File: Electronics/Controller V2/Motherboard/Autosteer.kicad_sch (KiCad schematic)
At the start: 12 parts, among them Q1 2N7002, Q2 2N7002, U11 ADS1115IDGS

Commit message: Added WAS circuit.
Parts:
- D5, D6: value D_Zener -> 1N5819WS; footprint (none) -> Diode_SMD:D_SOD-323; LCSC (none) -> C191023
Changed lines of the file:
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@@
       (effects (font (size 1.27 1.27)) (justify left))
     )
-    (property "Value" "D_Zener" (at 117.475 90.805 90)
-      (effects (font (size 1.27 1.27)) (justify left) hide)
+    (property "Value" "1N5819WS" (at 111.76 81.915 0)
+      (effects (font (size 1.27 1.27)) (justify left))
     )
-    (property "Footprint" "" (at 114.3 89.535 0)
+    (property "Footprint" "Diode_SMD:D_SOD-323" (at 114.3 89.535 0)
       (effects (font (size 1.27 1.27)) hide)
     )
     (property "Datasheet" "~" (at 114.3 89.535 0)
+      (effects (font (size 1.27 1.27)) hide)
+    )
+    (property "LCSC" "C191023" (at 114.3 89.535 0)
       (effects (font (size 1.27 1.27)) hide)
     )
@@
       (effects (font (size 1.27 1.27)) (justify left))
     )
-    (property "Value" "D_Zener" (at 125.73 90.805 90)
-      (effects (font (size 1.27 1.27)) (justify left) hide)
+    (property "Value" "1N5819WS" (at 120.015 81.915 0)
+      (effects (font (size 1.27 1.27)) (justify left))
     )
-    (property "Footprint" "" (at 122.555 89.535 0)
+    (property "Footprint" "Diode_SMD:D_SOD-323" (at 122.555 89.535 0)
       (effects (font (size 1.27 1.27)) hide)
     )
@@
       (effects (font (size 1.27 1.27)) hide)
     )
+    (property "LCSC" "C191023" (at 122.555 89.535 0)
+      (effects (font (size 1.27 1.27)) hide)
+    )

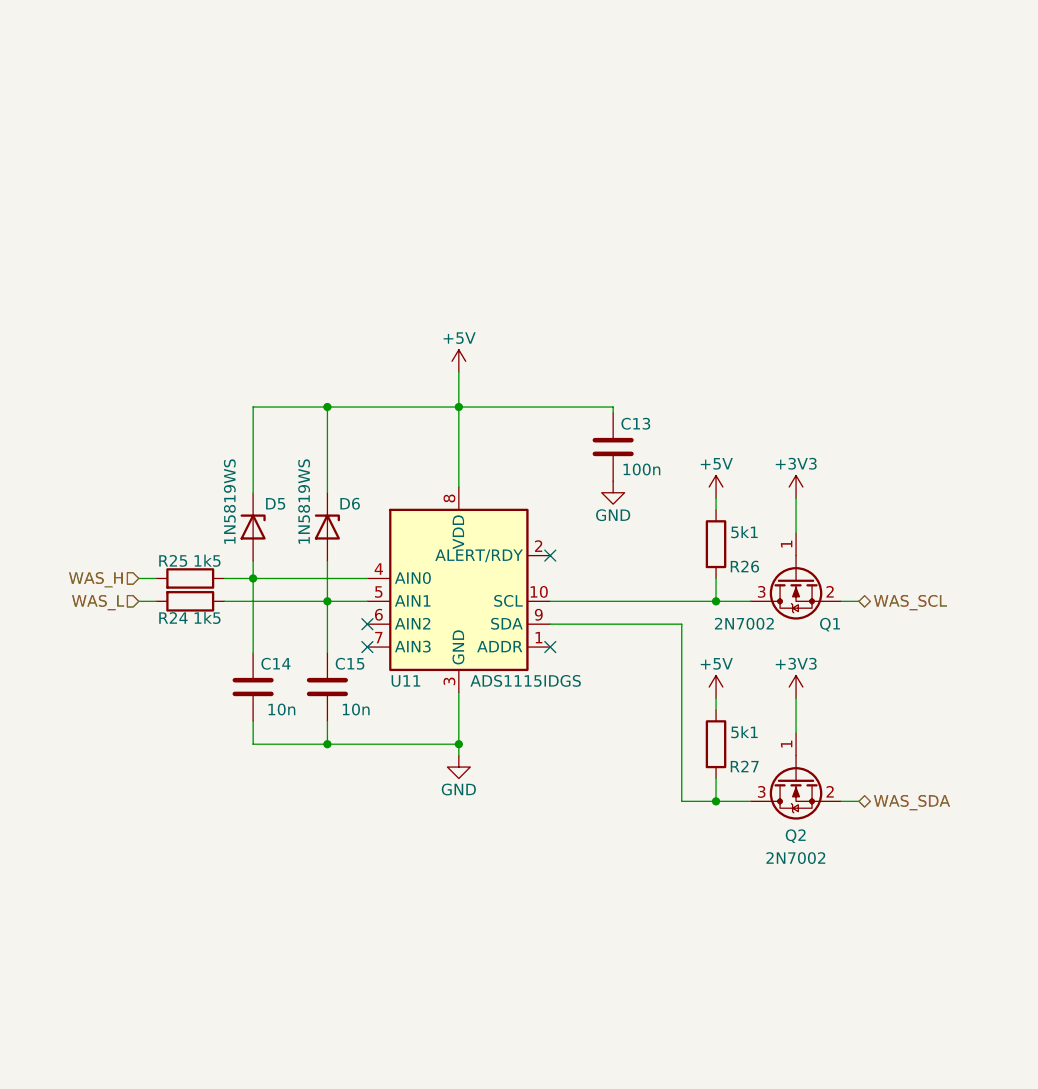
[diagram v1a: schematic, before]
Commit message: Added current sensing for valve E.
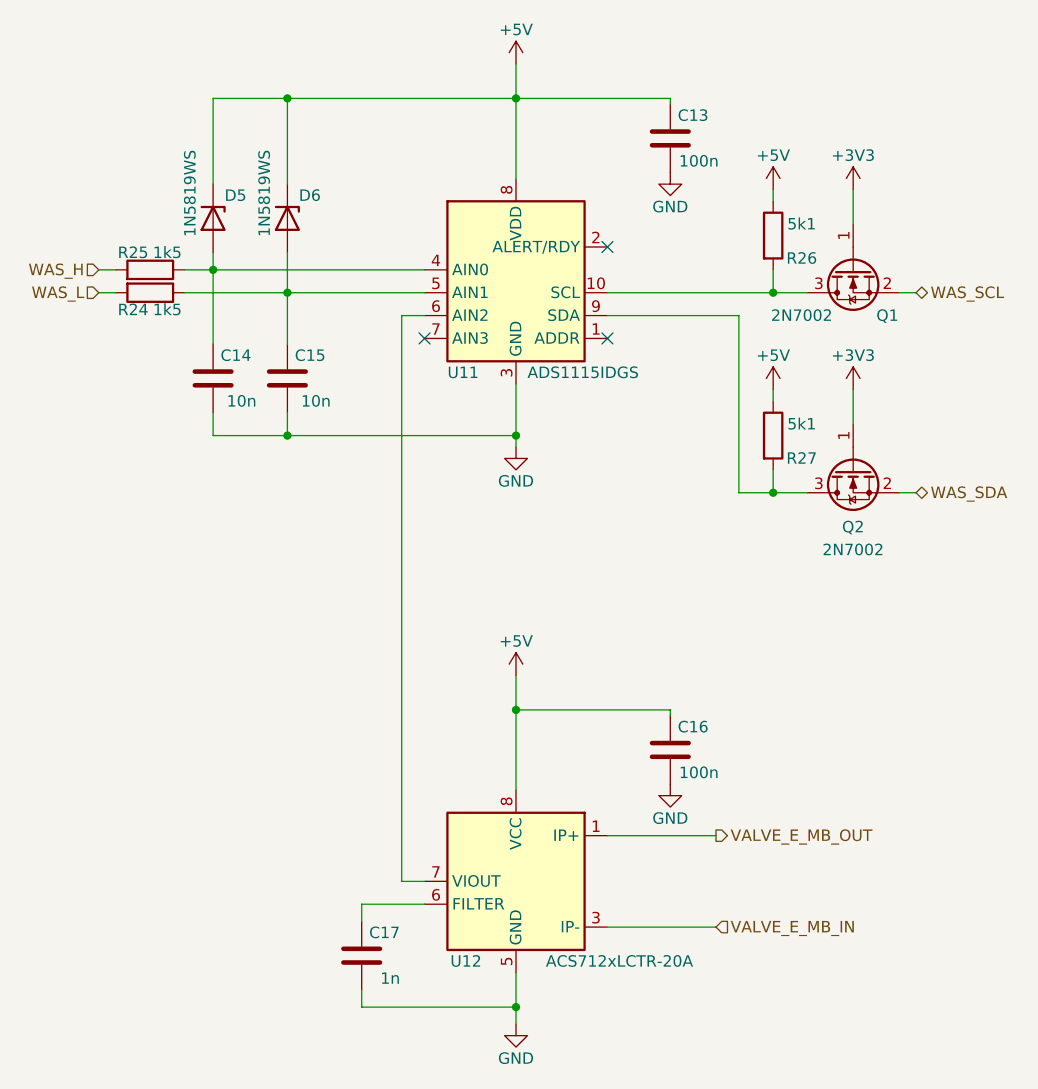
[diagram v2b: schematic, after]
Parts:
- added C16: 100n, Capacitor_SMD:C_0805_2012Metric, symbol Device:C
- added C17: 1n, Capacitor_SMD:C_0805_2012Metric, symbol Device:C
- added U12: ACS712xLCTR-20A, Package_SO:SOIC-8_3.9x4.9mm_P1.27mm, symbol Sensor_Current:ACS712xLCTR-20A
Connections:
- net +5V: now also C16.2, U12.8 (VCC)
- net GND: now also C16.1, C17.1, U12.5 (GND)
- net at U11.6 (AIN2): now also U12.7 (VIOUT)
- new net: C17.2, U12.6 (FILTER)
- new net VALVE_E_MB_IN: U12.3 (IP-), U12.4 (IP-)
- new net VALVE_E_MB_OUT: U12.1 (IP+), U12.2 (IP+)
- no-connect marks 4 -> 3
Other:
- moved on the sheet: C13, C14, C15, D5, D6, Q1, Q2, R24, R25, R26, R27, U11

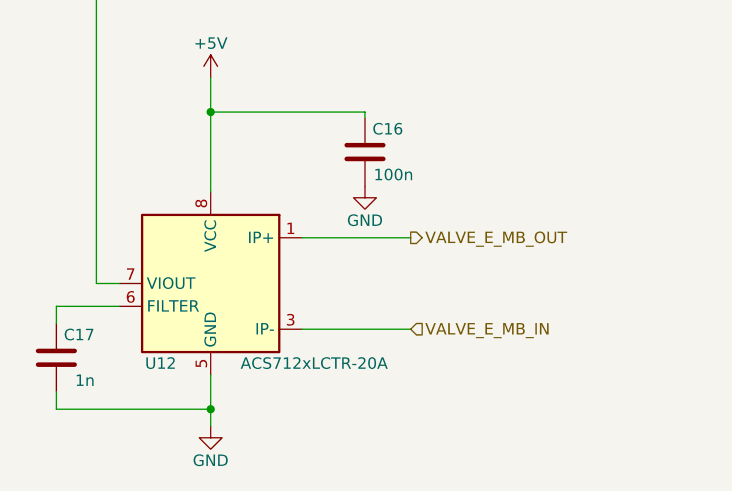
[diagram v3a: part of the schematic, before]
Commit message: Added jumper to bypass current sensing. Minor tweaks. Generated production files.
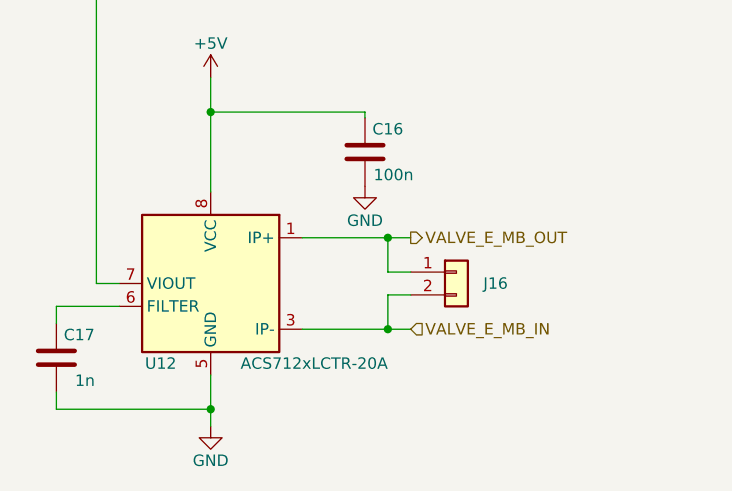
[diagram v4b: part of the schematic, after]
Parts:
- added J16: ~, Connector_PinHeader_2.54mm:PinHeader_1x02_P2.54mm_Vertical, symbol Connector_Generic:Conn_01x02
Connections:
- net VALVE_E_MB_IN: now also J16.2 (Pin_2)
- net VALVE_E_MB_OUT: now also J16.1 (Pin_1)
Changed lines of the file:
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@@
   (junction (at 109.855 60.96) (diameter 0) (color 0 0 0 0)
   )
+  (junction (at 163.195 123.825) (diameter 0) (color 0 0 0 0)
+  )
   (junction (at 143.51 142.875) (diameter 0) (color 0 0 0 0)
   )
@@
   )
   (junction (at 118.11 41.91) (diameter 0) (color 0 0 0 0)
+  )
+  (junction (at 163.195 133.985) (diameter 0) (color 0 0 0 0)
   )
   (junction (at 143.51 41.91) (diameter 0) (color 0 0 0 0)
@@
     (stroke (width 0) (type default))
   )
+  (wire (pts (xy 163.195 127.635) (xy 163.195 123.825))
+    (stroke (width 0) (type default))
+  )
   (wire (pts (xy 109.855 60.96) (xy 133.35 60.96))
     (stroke (width 0) (type default))
@@
     (stroke (width 0) (type default))
   )
-  (wire (pts (xy 153.67 123.825) (xy 165.735 123.825))
+  (wire (pts (xy 153.67 123.825) (xy 163.195 123.825))
     (stroke (width 0) (type default))
   )
@@
     (stroke (width 0) (type default))
   )
+  (wire (pts (xy 165.735 127.635) (xy 163.195 127.635))
+    (stroke (width 0) (type default))
+  )
   (wire (pts (xy 109.855 79.375) (xy 118.11 79.375))
     (stroke (width 0) (type default))
@@
     (stroke (width 0) (type default))
   )
-  (wire (pts (xy 153.67 133.985) (xy 165.735 133.985))
+  (wire (pts (xy 153.67 133.985) (xy 163.195 133.985))
     (stroke (width 0) (type default))
   )
@@
     (stroke (width 0) (type default))
   )
+  (wire (pts (xy 163.195 130.175) (xy 163.195 133.985))
+    (stroke (width 0) (type default))
+  )
   (wire (pts (xy 118.11 41.91) (xy 118.11 51.435))
     (stroke (width 0) (type default))
@@
     (stroke (width 0) (type default))
   )
+  (wire (pts (xy 163.195 133.985) (xy 165.735 133.985))
+    (stroke (width 0) (type default))
+  )
   (wire (pts (xy 186.055 85.725) (xy 187.96 85.725))
     (stroke (width 0) (type default))
@@
   )
   (wire (pts (xy 118.11 59.055) (xy 118.11 63.5))
+    (stroke (width 0) (type default))
+  )
+  (wire (pts (xy 165.735 130.175) (xy 163.195 130.175))
+    (stroke (width 0) (type default))
+  )
+  (wire (pts (xy 163.195 123.825) (xy 165.735 123.825))
     (stroke (width 0) (type default))
   )
@@
         )
       )
+    )
+  )
+  (symbol (lib_id "Connector_Generic:Conn_01x02") (at 170.815 127.635 0) (unit 1)
+    (in_bom yes) (on_board yes) (dnp no)
+    (property "Reference" "J16" (at 176.53 128.905 0)
+      (effects (font (size 1.27 1.27)) (justify right))
+    )
+    (property "Value" "~" (at 179.07 129.54 0)
+      (effects (font (size 1.27 1.27)) (justify right) hide)
+    )
+    (property "Footprint" "Connector_PinHeader_2.54mm:PinHeader_1x02_P2.54mm_Vertical" (at 170.815 127.635 0)
+      (effects (font (size 1.27 1.27)) hide)
+    )
+    (property "Datasheet" "~" (at 170.815 127.635 0)
+      (effects (font (size 1.27 1.27)) hide)
+    )
+    (property "LCSC" "C7494857" (at 170.815 127.635 0)
+      (effects (font (size 1.27 1.27)) hide)
+    )
+    (pin "1")
+    (pin "2")
+    (instances
+      (project "Tandem Leveller Controller V2"
+        (path "/dceffac9-8f5b-4889-8265-b6c471cb5dde/f43c4e36-971b-41e2-adc7-d90929e38a42"
+          (reference "J16") (unit 1)
+        )
+      )
